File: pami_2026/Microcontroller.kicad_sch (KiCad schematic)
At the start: 11 parts, among them U1 ESP32-WROOM-E

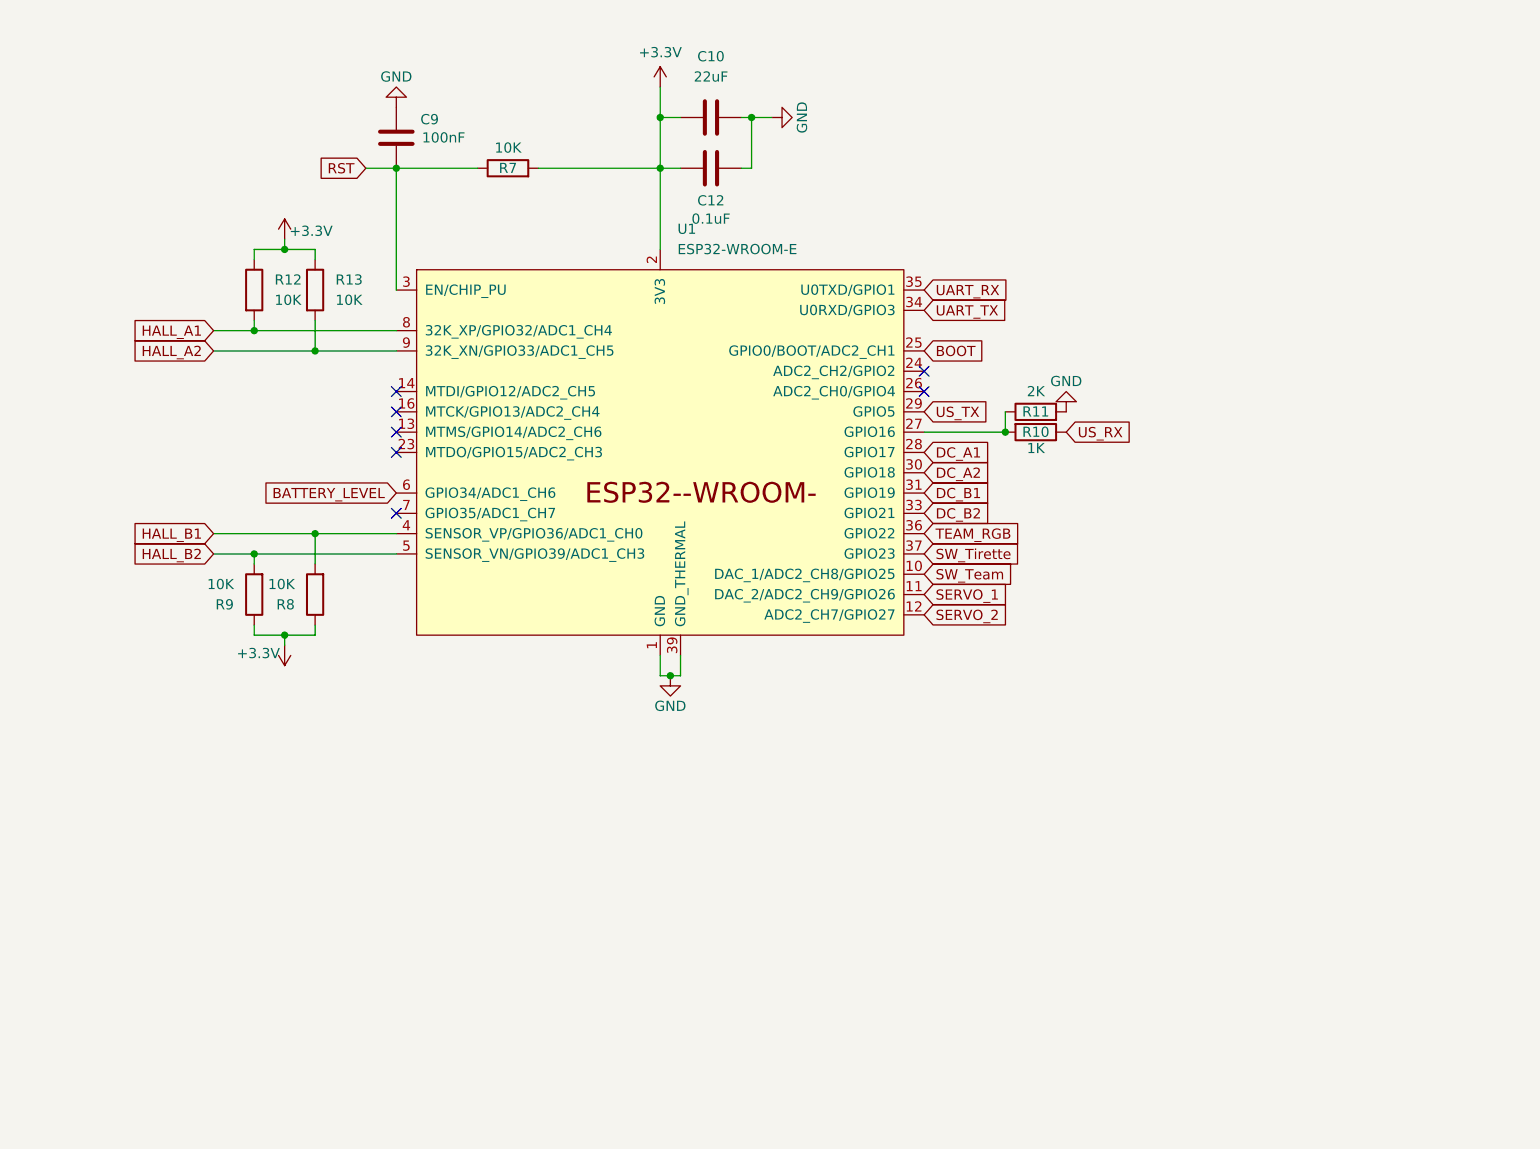
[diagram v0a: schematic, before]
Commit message: Fix: ERC is Happy - proper footprints - Feat: add multiplexer for external power
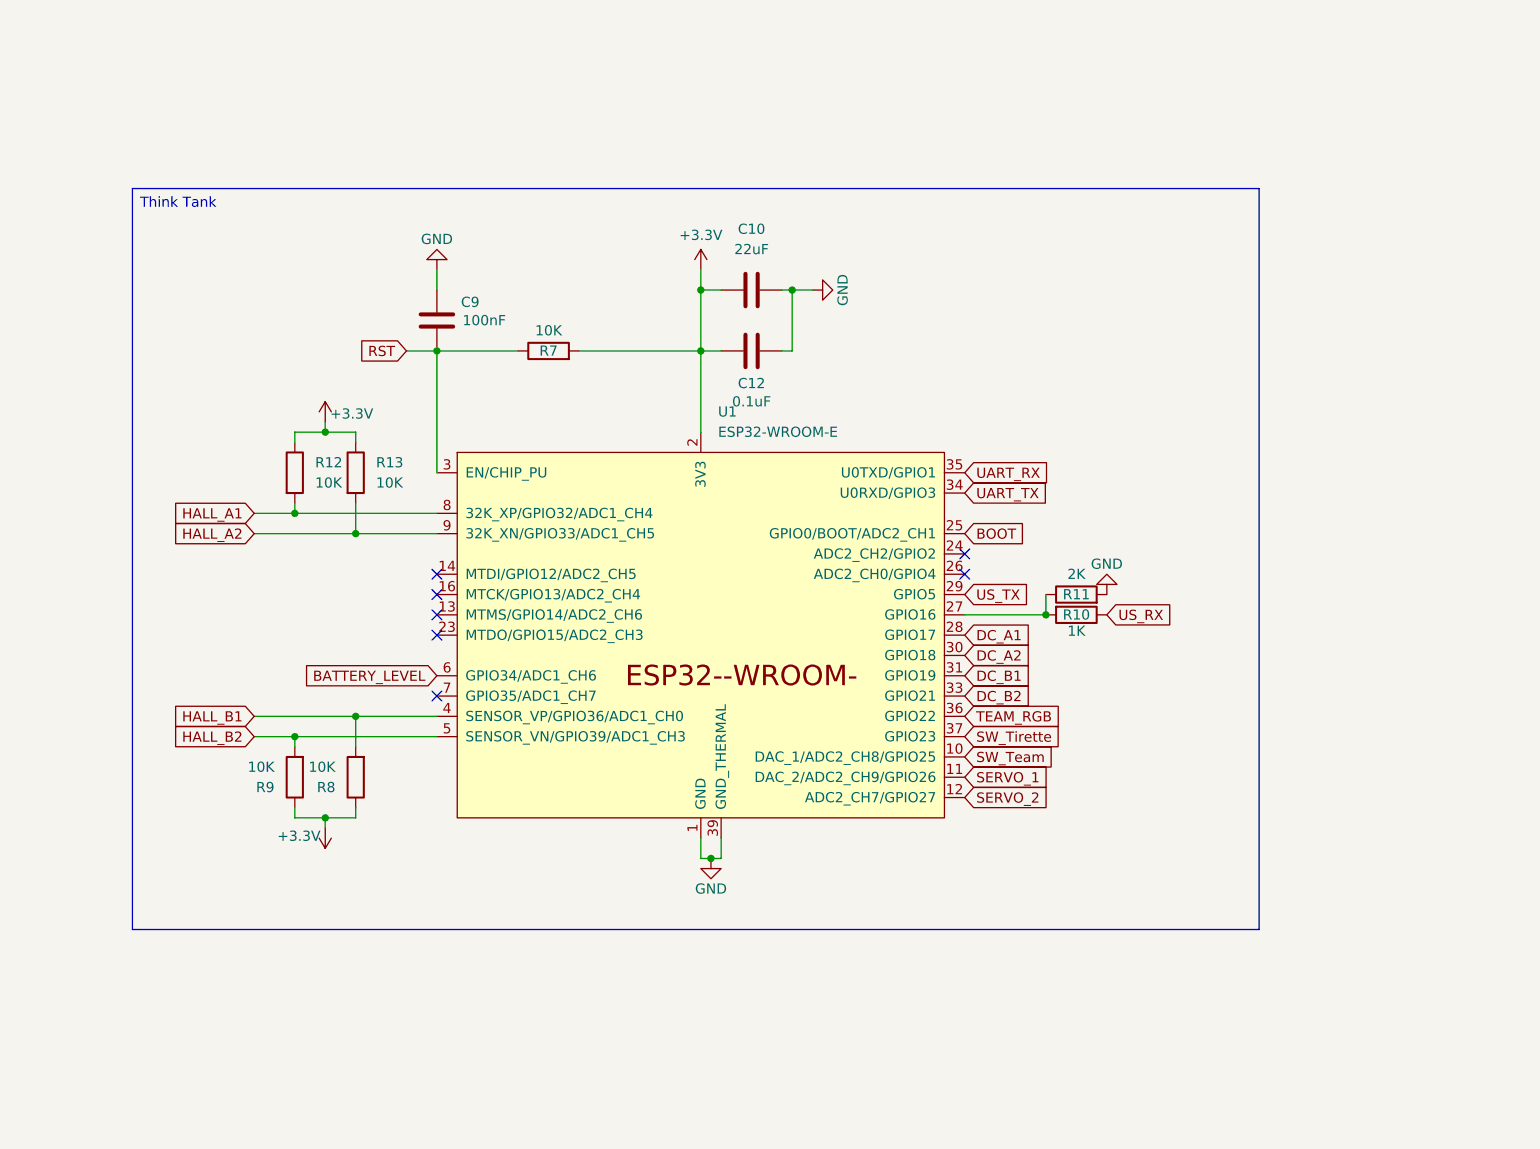
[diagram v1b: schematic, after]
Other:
- moved on the sheet: C10, C12, C9, R10, R11, R12, R13, R7, R8, R9, U1

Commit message: fix strapping pin
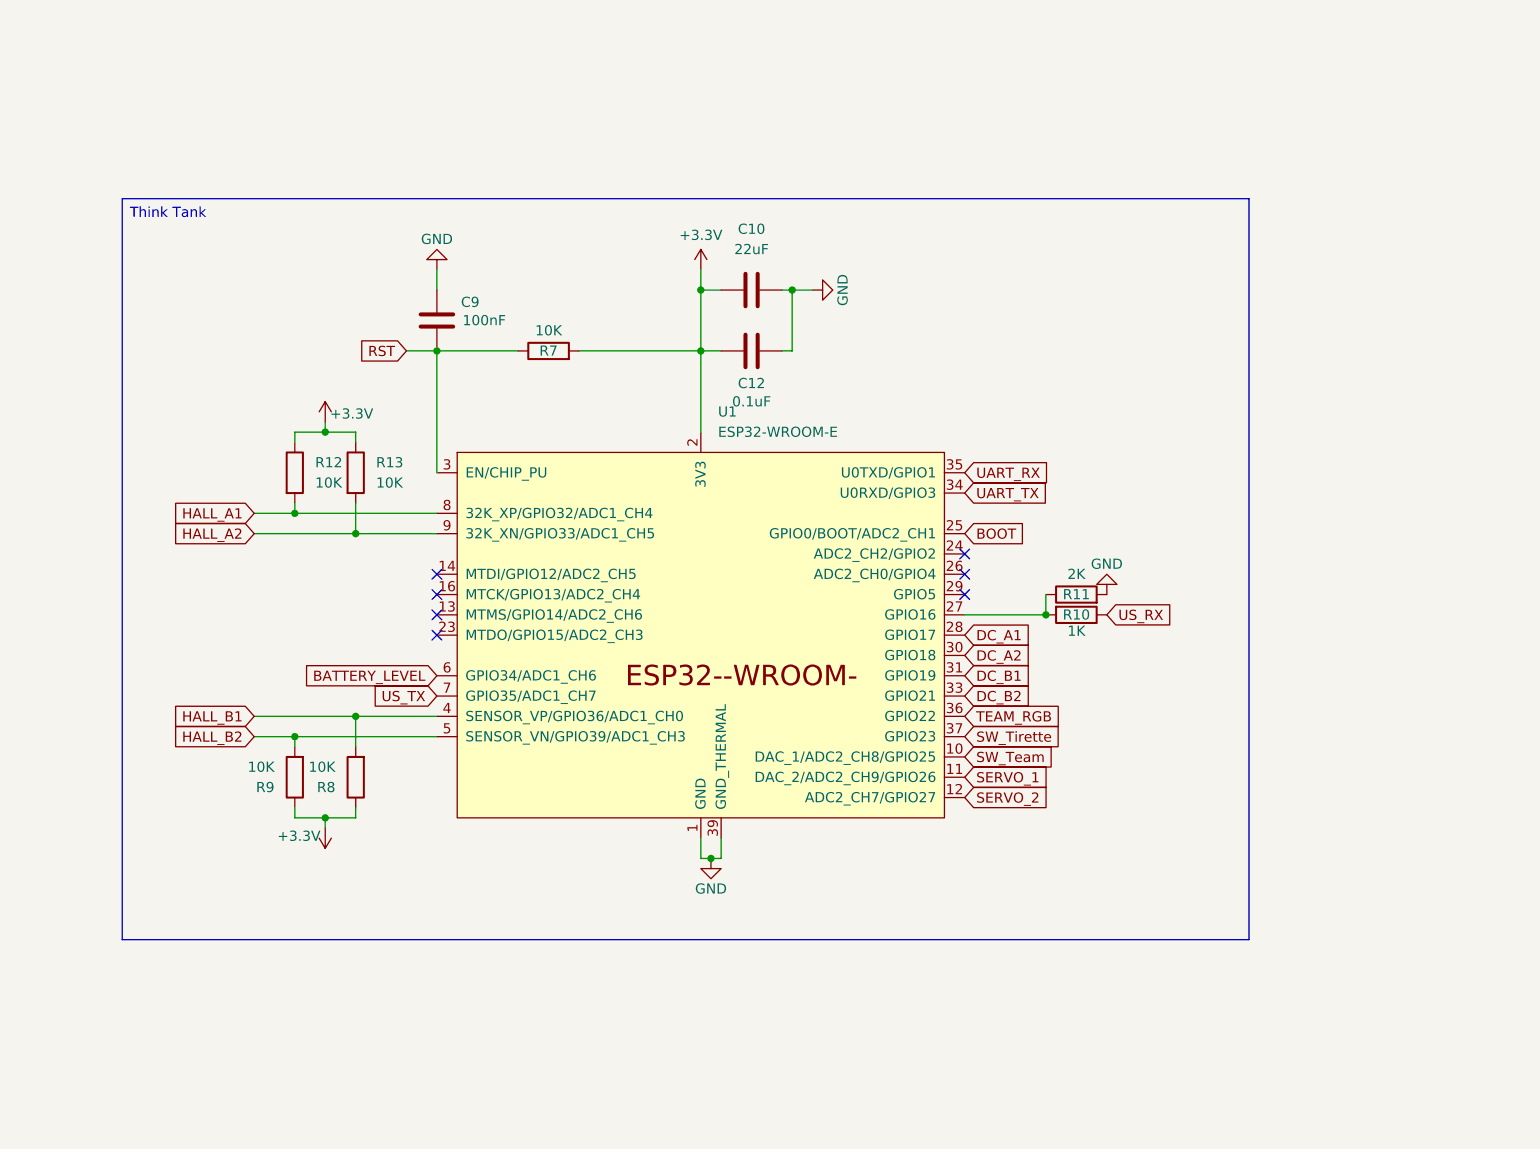
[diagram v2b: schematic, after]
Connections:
- net US_TX: now also U1.7 (GPIO35/ADC1_CH7); no longer U1.29 (GPIO5)
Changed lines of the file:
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@@
 	(text_box "Think Tank"
 		(exclude_from_sim no)
-		(at 77.47 50.8 0)
+		(at 76.2 52.07 0)
 		(size 140.97 92.71)
 		(margins 0.9525 0.9525 0.9525 0.9525)
@@
 	)
 	(no_connect
+		(at 181.61 99.06)
+	)
+	(no_connect
 		(at 115.57 99.06)
 	)
@@
 	)
 	(no_connect
-		(at 181.61 99.06)
-	)
-	(no_connect
 		(at 115.57 104.14)
 	)
@@
 	)
 	(no_connect
-		(at 115.57 114.3)
+		(at 181.61 101.6)
 	)
 	(no_connect
@@
 		)
 	)
+	(global_label "US_TX"
+		(shape input)
+		(at 115.57 114.3 180)
+		(fields_autoplaced yes)
+		(effects
+			(font
+				(size 1.27 1.27)
+			)
+			(justify right)
+		)
+		(property "Intersheetrefs" "${INTERSHEET_REFS}"
+			(at 106.9001 114.3 0)
+			(effects
+				(font
+					(size 1.27 1.27)
+				)
+				(justify right)
+				(hide yes)
+			)
+		)
+	)
 	(global_label "HALL_A2"
 		(shape input)
@@
 				(hide yes)
 			)
-		)
-	)
-	(global_label "US_TX"
-		(shape input)
-		(at 181.61 101.6 0)
-		(fields_autoplaced yes)
-		(effects
-			(font
-				(size 1.27 1.27)
-			)
-			(justify left)
-		)
-		(property "Intersheetrefs" "${INTERSHEET_REFS}"
-			(at 190.2799 101.6 0)
-			(effects
-				(font
-					(size 1.27 1.27)
-				)
-				(justify left)
-				(hide yes)
-			)

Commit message: FEAT : Routing
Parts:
- U1: footprint PCM_Espressif:ESP32-WROOM-32E -> lib:ESP32-WROOM-32E
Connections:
- net STATUS_ESP: now reaches U1.26 (ADC2_CH0/GPIO4)
- no-connect marks 7 -> 6
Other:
- moved on the sheet: R10, R11
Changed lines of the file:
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@@
 	(text_box "Think Tank"
 		(exclude_from_sim no)
-		(at 76.2 52.07 0)
+		(at 73.66 49.53 0)
 		(size 140.97 92.71)
 		(margins 0.9525 0.9525 0.9525 0.9525)
@@
 	)
 	(junction
-		(at 191.77 104.14)
+		(at 194.31 104.14)
 		(diameter 0)
 		(color 0 0 0 0)
@@
 	)
 	(no_connect
-		(at 181.61 99.06)
-	)
-	(no_connect
 		(at 115.57 99.06)
 	)
@@
 	(wire
 		(pts
-			(xy 191.77 104.14) (xy 191.77 101.6)
+			(xy 194.31 104.14) (xy 194.31 101.6)
+		)
+		(stroke
+			(width 0)
+			(type default)
+		)
+	)
+	(wire
+		(pts
+			(xy 181.61 104.14) (xy 194.31 104.14)
 		)
 		(stroke
@@
 		(pts
 			(xy 101.6 80.01) (xy 101.6 81.28)
-		)
-		(stroke
-			(width 0)
-			(type default)
-		)
-	)
-	(wire
-		(pts
-			(xy 181.61 104.14) (xy 191.77 104.14)
 		)
 		(stroke
@@
 		)
 	)
+	(global_label "STATUS_ESP"
+		(shape input)
+		(at 181.61 99.06 0)
+		(fields_autoplaced yes)
+		(effects
+			(font
+				(size 1.27 1.27)
+			)
+			(justify left)
+		)
+		(property "Intersheetrefs" "${INTERSHEET_REFS}"
+			(at 195.9646 99.06 0)
+			(effects
+				(font
+					(size 1.27 1.27)
+				)
+				(justify left)
+				(hide yes)
+			)
+		)
+	)
 	(global_label "SW_Team"
 		(shape input)
@@
 	(global_label "US_RX"
 		(shape input)
-		(at 199.39 104.14 0)
+		(at 201.93 104.14 0)
 		(fields_autoplaced yes)
 		(effects
@@
 		)
 		(property "Intersheetrefs" "${INTERSHEET_REFS}"
-			(at 208.3623 104.14 0)
+			(at 210.9023 104.14 0)
 			(effects
 				(font
@@
 	(symbol
 		(lib_id "Device:R")
-		(at 195.58 104.14 270)
+		(at 198.12 104.14 270)
 		(unit 1)
 		(exclude_from_sim no)
@@
 		(dnp no)
 		(property "Reference" "R10"
-			(at 195.58 104.14 90)
+			(at 198.12 104.14 90)
 			(effects
 				(font
@@
 		)
 		(property "Value" "1K"
-			(at 195.58 106.172 90)
+			(at 198.12 106.172 90)
 			(effects
 				(font
@@
 		)
 		(property "Footprint" "Resistor_SMD:R_0603_1608Metric"
-			(at 195.58 102.362 90)
+			(at 198.12 102.362 90)
 			(effects
 				(font
@@
 		)
 		(property "Datasheet" "~"
-			(at 195.58 104.14 0)
+			(at 198.12 104.14 0)
 			(effects
 				(font
@@
 		)
 		(property "Description" "Resistor"
-			(at 195.58 104.14 0)
+			(at 198.12 104.14 0)
 			(effects
 				(font
@@
 	(symbol
 		(lib_id "PCM_SparkFun-PowerSymbol:GND")
-		(at 199.39 101.6 180)
+		(at 201.93 101.6 180)
 		(unit 1)
 		(exclude_from_sim no)
@@
 		(fields_autoplaced yes)
 		(property "Reference" "#PWR050"
-			(at 199.39 95.25 0)
+			(at 201.93 95.25 0)
 			(effects
 				(font
@@
 		)
 		(property "Value" "GND"
-			(at 199.39 97.79 0)
+			(at 201.93 97.79 0)
 			(do_not_autoplace yes)
 			(effects
@@
 		)
 		(property "Footprint" ""
-			(at 199.39 101.6 0)
+			(at 201.93 101.6 0)
 			(effects
 				(font
@@
 		)
 		(property "Datasheet" ""
-			(at 199.39 101.6 0)
+			(at 201.93 101.6 0)
 			(effects
 				(font
@@
 		)
 		(property "Description" "Power symbol creates a global label with name \"GND\" , ground"
-			(at 199.39 92.71 0)
+			(at 201.93 92.71 0)
 			(effects
 				(font
@@
 	(symbol
 		(lib_id "Device:R")
-		(at 195.58 101.6 90)
+		(at 198.12 101.6 90)
 		(unit 1)
 		(exclude_from_sim no)
@@
 		(dnp no)
 		(property "Reference" "R11"
-			(at 195.58 101.6 90)
+			(at 198.12 101.6 90)
 			(effects
 				(font
@@
 		)
 		(property "Value" "2K"
-			(at 195.58 99.06 90)
+			(at 198.12 99.06 90)
 			(effects
 				(font
@@
 		)
 		(property "Footprint" "Resistor_SMD:R_0603_1608Metric"
-			(at 195.58 103.378 90)
+			(at 198.12 103.378 90)
 			(effects
 				(font
@@
 		)
 		(property "Datasheet" "~"
-			(at 195.58 101.6 0)
+			(at 198.12 101.6 0)
 			(effects
 				(font
@@
 		)
 		(property "Description" "Resistor"
-			(at 195.58 101.6 0)
+			(at 198.12 101.6 0)
 			(effects
 				(font
@@
 			)
 		)
-		(property "Footprint" "PCM_Espressif:ESP32-WROOM-32E"
+		(property "Footprint" "lib:ESP32-WROOM-32E"
 			(at 148.59 142.24 0)
 			(effects

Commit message: Feat: BOM LCSC + big plan de masse
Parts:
- C10: LCSC (none) -> C602037
- C12, C9: LCSC (none) -> C1591
- R10: LCSC (none) -> C22548
- R11: LCSC (none) -> C105576
- R12, R13, R7, R8, R9: LCSC (none) -> C98220
- U1: LCSC (none) -> C701343
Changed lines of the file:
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@@
+			)
+		)
+		(property "LCSC" "C22548"
+			(at 198.12 104.14 90)
+			(effects
+				(font
+					(size 1.27 1.27)
+				)
+				(hide yes)
 			)
 		)
@@
 		)
 		(property "Description" "Unpolarized capacitor"
+			(at 115.57 67.31 0)
+			(effects
+				(font
+					(size 1.27 1.27)
+				)
+				(hide yes)
+			)
+		)
+		(property "LCSC" "C1591"
 			(at 115.57 67.31 0)
 			(effects
@@
 			)
 		)
+		(property "LCSC" "C98220"
+			(at 105.41 124.46 0)
+			(effects
+				(font
+					(size 1.27 1.27)
+				)
+				(hide yes)
+			)
+		)
 		(pin "2"
 		)
@@
 			)
 		)
+		(property "LCSC" "C98220"
+			(at 97.79 124.46 0)
+			(effects
+				(font
+					(size 1.27 1.27)
+				)
+				(hide yes)
+			)
+		)
 		(pin "2"
 		)
@@
 			)
 		)
+		(property "LCSC" "C602037"
+			(at 154.94 63.5 90)
+			(effects
+				(font
+					(size 1.27 1.27)
+				)
+				(hide yes)
+			)
+		)
 		(pin "2"
 		)
@@
 			)
 		)
+		(property "LCSC" "C1591"
+			(at 154.94 71.12 90)
+			(effects
+				(font
+					(size 1.27 1.27)
+				)
+				(hide yes)
+			)
+		)
 		(pin "2"
 		)
@@
 			)
 		)
+		(property "LCSC" "C98220"
+			(at 97.79 86.36 0)
+			(effects
+				(font
+					(size 1.27 1.27)
+				)
+				(hide yes)
+			)
+		)
 		(pin "2"
 		)
@@
 			)
 		)
+		(property "LCSC" "C98220"
+			(at 129.54 71.12 90)
+			(effects
+				(font
+					(size 1.27 1.27)
+				)
+				(hide yes)
+			)
+		)
 		(pin "2"
 		)
@@
 		(property "Description" "Resistor"
 			(at 198.12 101.6 0)
+			(effects
+				(font
+					(size 1.27 1.27)
+				)
+				(hide yes)
+			)
+		)
+		(property "LCSC" "C105576"
+			(at 198.12 101.6 90)
 			(effects
 				(font
@@
 			)
 		)
+		(property "LCSC" "C98220"
+			(at 105.41 86.36 0)
+			(effects
+				(font
+					(size 1.27 1.27)
+				)
+				(hide yes)
+			)
+		)
 		(pin "2"
 		)
@@
 			(at 148.59 106.68 0)
 			(effects
+				(font
+					(size 1.27 1.27)
+				)
+				(hide yes)
+			)
+		)
+		(property "LCSC" "C701343"
+			(at 148.59 106.68 0)
+			(effects

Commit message: Cleanup
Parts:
- added SERVO_1, SERVO_2, TEAM_RGB: Conn_01x03_Pin, Connector_PinHeader_2.54mm:PinHeader_1x03_P2.54mm_Vertical, symbol Connector:Conn_01x03_Pin
- added SW1: SW_Reed, Connector_PinHeader_2.54mm:PinHeader_1x02_P2.54mm_Vertical, symbol Switch:SW_Reed
- added SWPushBoot1, SWPushReset1: SMD_6.2x6.2mm_h7.0mm, PCM_SparkFun-Switch:Push_SMD_6.2x6.2mm, symbol PCM_SparkFun-Switch:SPST_Push_SMD_6.2x6.2mm_h7.0mm
- added SW_TEAM: Conn_01x02_Pin, Connector_PinHeader_2.54mm:PinHeader_1x02_P2.54mm_Vertical, symbol Connector:Conn_01x02_Pin
- added UART, US: Conn_01x04_Pin, Connector_PinHeader_2.54mm:PinHeader_1x04_P2.54mm_Vertical, symbol Connector:Conn_01x04_Pin
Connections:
- net BOOT: now also SWPushBoot1.1
- net GND: now also SERVO_1.1 (Pin_1), SERVO_2.1 (Pin_1), SW1.2, SWPushBoot1.2, SWPushReset1.2, SW_TEAM.1 (Pin_1), TEAM_RGB.3 (Pin_3), UART.4 (Pin_4), US.1 (Pin_1)
- net RST: now also SWPushReset1.1
- net SERVO_1: now also SERVO_1.2 (Pin_2)
- net SERVO_2: now also SERVO_2.2 (Pin_2)
- net SW_Team: now also SW_TEAM.2 (Pin_2)
- net SW_Tirette: now also SW1.1
- net TEAM_RGB: now also TEAM_RGB.2 (Pin_2)
- net UART_RX: now also UART.3 (Pin_3)
- net UART_TX: now also UART.2 (Pin_2)
- net US_RX: now also US.2 (Pin_2)
- net US_TX: now also US.3 (Pin_3)
- new net +5V: SERVO_1.3 (Pin_3), SERVO_2.3 (Pin_3), TEAM_RGB.1 (Pin_1), US.4 (Pin_4)
- new net EXTERNAL: UART.1 (Pin_1)
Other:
- moved on the sheet: C10, C12, C9, R10, R11, R7, R8, R9

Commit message: Fixes and updates to v2
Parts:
- renumbered SW_TEAM to SW_TEAM1, TEAM_RGB to TEAM_RGB1, UART to UART1, US to US1
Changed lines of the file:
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@@
 		(dnp no)
 		(fields_autoplaced yes)
-		(property "Reference" "SW_TEAM"
+		(property "Reference" "SW_TEAM1"
 			(at 87.63 158.1149 90)
 			(effects
@@
 			(project "pami_2026"
 				(path "/2e16a05b-e8ca-4fff-9c3e-5c880745daa6/56f8c084-7953-4857-a452-d40cb21fa6ff"
-					(reference "SW_TEAM")
+					(reference "SW_TEAM1")
 					(unit 1)
 				)
@@
 		(dnp no)
 		(fields_autoplaced yes)
-		(property "Reference" "US"
+		(property "Reference" "US1"
 			(at 233.68 64.7699 0)
 			(effects
@@
 			(project "pami_2026"
 				(path "/2e16a05b-e8ca-4fff-9c3e-5c880745daa6/56f8c084-7953-4857-a452-d40cb21fa6ff"
-					(reference "US")
+					(reference "US1")
 					(unit 1)
 				)
@@
 		(dnp no)
 		(fields_autoplaced yes)
-		(property "Reference" "UART"
+		(property "Reference" "UART1"
 			(at 134.62 38.0999 0)
 			(effects
@@
 			(project "pami_2026"
 				(path "/2e16a05b-e8ca-4fff-9c3e-5c880745daa6/56f8c084-7953-4857-a452-d40cb21fa6ff"
-					(reference "UART")
+					(reference "UART1")
 					(unit 1)
 				)
@@
 		(dnp no)
 		(fields_autoplaced yes)
-		(property "Reference" "TEAM_RGB"
+		(property "Reference" "TEAM_RGB1"
 			(at 220.98 102.87 90)
 			(effects
@@
 			(project "pami_2026"
 				(path "/2e16a05b-e8ca-4fff-9c3e-5c880745daa6/56f8c084-7953-4857-a452-d40cb21fa6ff"
-					(reference "TEAM_RGB")
-					(unit 1)
-				)
+					(reference "TEAM_RGB1")
+					(unit 1)
+				)
